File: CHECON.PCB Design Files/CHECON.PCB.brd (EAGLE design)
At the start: 81.7 x 51.6 mm, 71 parts, among them T1 BC849, U2 MAX232SOIC16, U3 RS485SOIC, X1 53047-02

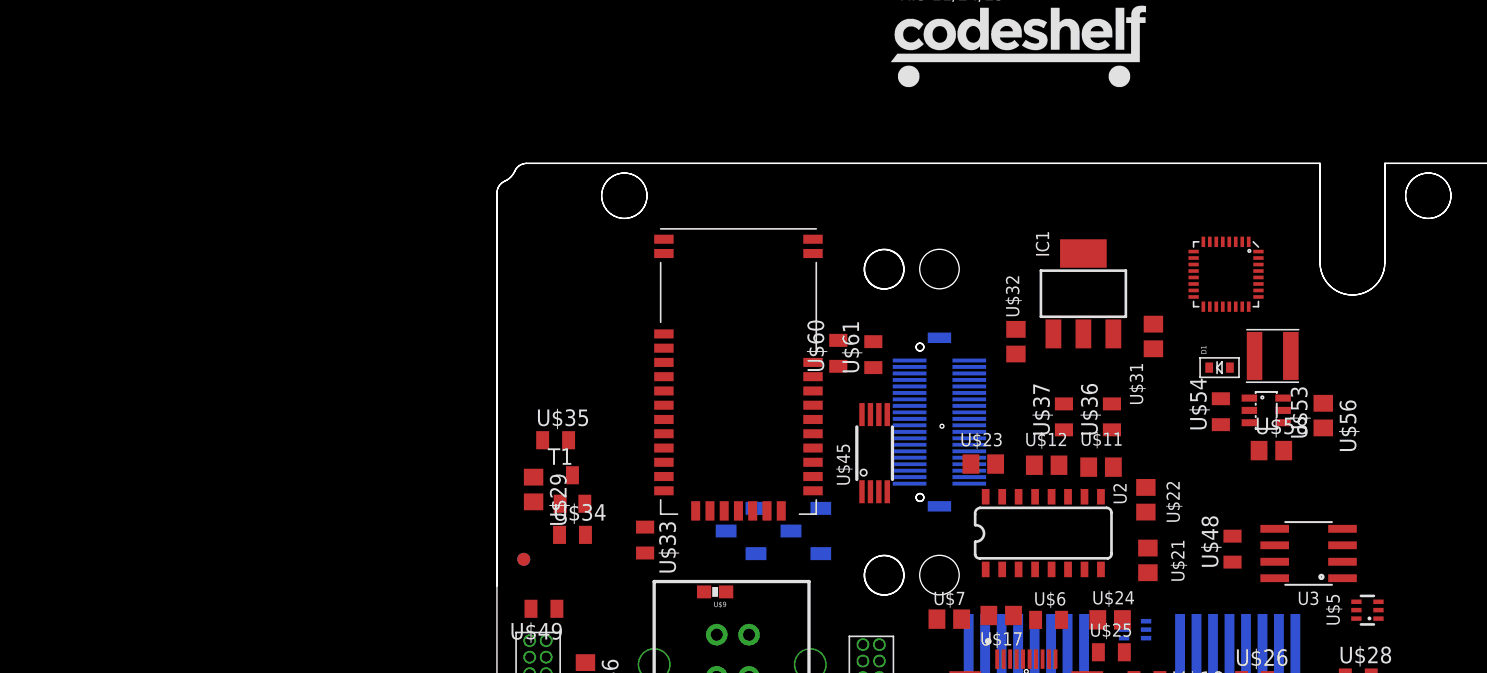
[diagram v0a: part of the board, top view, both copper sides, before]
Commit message: Updated KW2 footprint in design
Swapped footprint for one with 3mm foam outline
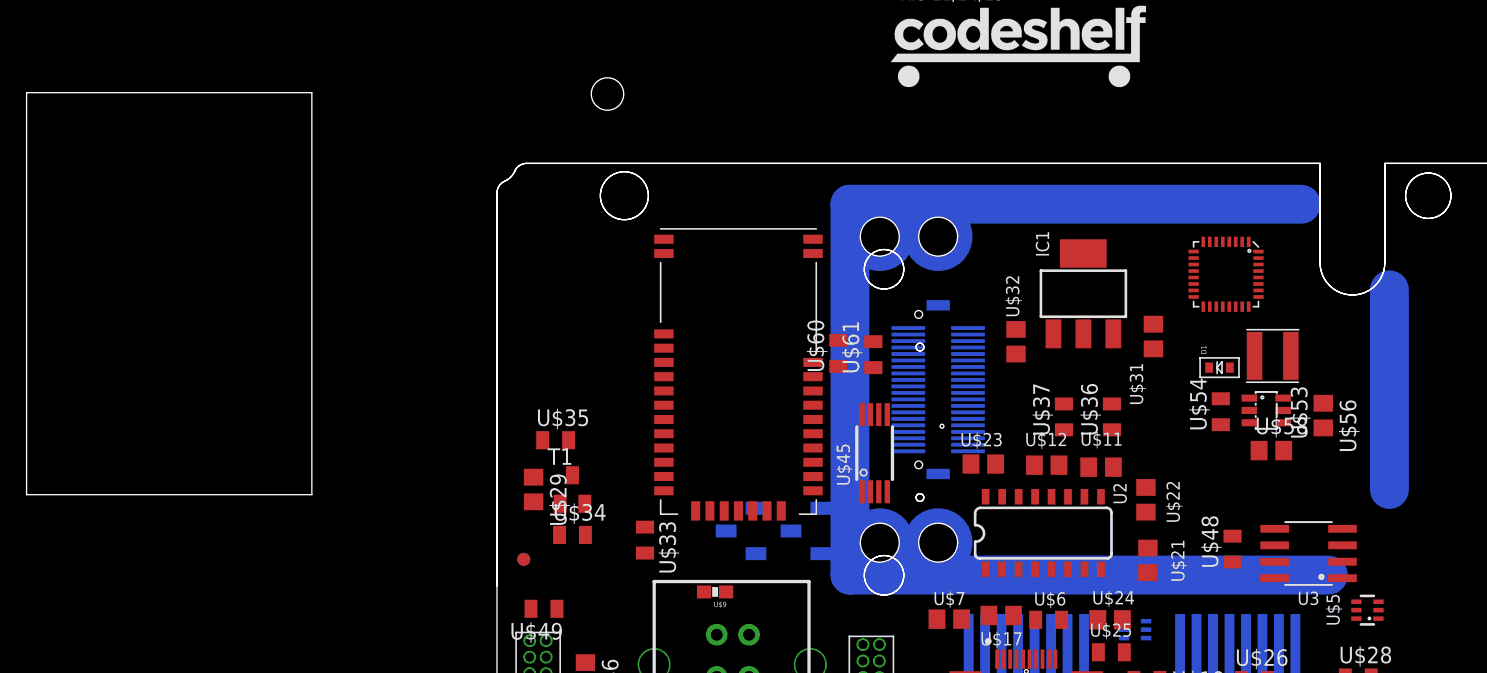
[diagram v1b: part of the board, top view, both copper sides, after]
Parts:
- U$10: value KW2_CPU_COMBO -> KW2_CPU_OFFSET; device KW2:BRAIN_COMBO -> KW2:BRAIN_OFFSET
- moved U$10 2.50 mm to (-6.80, -9.80)
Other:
- board size 81.7 x 51.6 mm -> 117.9 x 57.1 mm

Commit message: sync repo
Sync work while rafael was out
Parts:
- moved U$57 127.9 mm to (-129.6, -88.9)
- moved U$3 68.9 mm to (-46.0, -32.1), turned to 90 degrees
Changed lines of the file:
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@@
 <attribute name="MFGP" value="XD2B-0406-26A" x="-22.8" y="-40.9" size="1.778" layer="27" display="off"/>
 </element>
-<element name="U$3" library="KW2" package="QFN-32" value="KL20" x="15.4" y="-0.9" rot="R270">
-<attribute name="MFGN" value="Freescale" x="15.4" y="-0.9" size="1.778" layer="27" rot="R270" display="off"/>
-<attribute name="MFGP" value="MK20DX128VFM5" x="15.4" y="-0.9" size="1.778" layer="27" rot="R270" display="off"/>
+<element name="U$3" library="KW2" package="QFN-32" value="KL20" x="-46" y="-32.1" rot="R90">
+<attribute name="MFGN" value="Freescale" x="-46" y="-32.1" size="1.778" layer="27" rot="R90" display="off"/>
+<attribute name="MFGP" value="MK20DX128VFM5" x="-46" y="-32.1" size="1.778" layer="27" rot="R90" display="off"/>
 </element>
 <element name="U$9" library="SparkFun" package="0603-RES" value="TVS0603" x="-24" y="-25.4" rot="R180">
@@
 <attribute name="MFGP" value="RC0805FR-0715RL" x="9.3" y="-32.2" size="1.778" layer="27" rot="R180" display="off"/>
 </element>
-<element name="U$57" library="KW2" package="BM78" value="BM78" x="-22.2" y="-19.4"/>
+<element name="U$57" library="KW2" package="BM78" value="BM78" x="-129.6" y="-88.9"/>
 </elements>
 <signals>
@@
 <contactref element="JP1" pad="P$10"/>
 <contactref element="U$3" pad="21"/>
+<wire x1="-12.6" y1="-29.46" x2="-46.25" y2="-29.6" width="0" layer="19" extent="1-1"/>
 <wire x1="-4.5" y1="-6.05" x2="-12.6" y2="-29.46" width="0" layer="19" extent="16-16"/>
-<wire x1="15.65" y1="-3.4" x2="-4.5" y2="-6.05" width="0" layer="19" extent="1-16"/>
-<wire x1="36.9" y1="-36.4" x2="15.65" y2="-3.4" width="0" layer="19" extent="1-1"/>
-<wire x1="30.05" y1="-42.2" x2="36.9" y2="-36.4" width="0" layer="19" extent="1-1"/>
+<wire x1="30.05" y1="-42.2" x2="-12.6" y2="-29.46" width="0" layer="19" extent="1-1"/>
+<wire x1="36.9" y1="-36.4" x2="30.05" y2="-42.2" width="0" layer="19" extent="1-1"/>
 </signal>
 <signal name="GND" class="2">
@@
 <contactref element="U$57" pad="P$2"/>
 <contactref element="U$57" pad="P$3"/>
+<wire x1="-135.35" y1="-68.8" x2="-135.35" y2="-75" width="0" layer="19" extent="1-1"/>
+<wire x1="-135.35" y1="-67.7" x2="-135.35" y2="-68.8" width="0" layer="19" extent="1-1"/>
+<wire x1="-123.85" y1="-68.8" x2="-135.35" y2="-68.8" width="0" layer="19" extent="1-1"/>
+<wire x1="-123.85" y1="-67.7" x2="-123.85" y2="-68.8" width="0" layer="19" extent="1-1"/>
+<wire x1="-123.85" y1="-77.2" x2="-123.85" y2="-68.8" width="0" layer="19" extent="1-1"/>
+<wire x1="-36.3" y1="-39.765" x2="-123.85" y2="-67.7" width="0" layer="19" extent="1-1"/>
 <wire x1="-37.03" y1="-32.97" x2="-36.3" y2="-39.765" width="0" layer="19" extent="1-1"/>
 <wire x1="-37.03" y1="-31.7" x2="-37.03" y2="-32.97" width="0" layer="19" extent="1-1"/>
@@
 <wire x1="2.0886" y1="-5.4988" x2="9.8" y2="-4.75" width="0" layer="19" extent="1-1"/>
 <wire x1="-0.8" y1="-7.05" x2="2.0886" y2="-5.4988" width="0" layer="19" extent="1-1"/>
-<wire x1="-4.5" y1="-5.05" x2="-0.8" y2="-7.05" width="0" layer="19" extent="1-16"/>
-<wire x1="-4.5" y1="-5.55" x2="-4.5" y2="-5.05" width="0" layer="19" extent="16-16"/>
+<wire x1="-4.5" y1="-5.55" x2="-0.8" y2="-7.05" width="0" layer="19" extent="1-16"/>
+<wire x1="-4.5" y1="-5.05" x2="-4.5" y2="-5.55" width="0" layer="19" extent="16-16"/>
 <wire x1="-9.1" y1="-5.55" x2="-4.5" y2="-5.55" width="0" layer="19" extent="16-16"/>
 <wire x1="-9.1" y1="-5.05" x2="-9.1" y2="-5.55" width="0" layer="19" extent="16-16"/>
 <wire x1="-10.7232" y1="-11.7236" x2="-9.1" y2="-5.55" width="0" layer="19" extent="1-16"/>
-<wire x1="-16.45" y1="-7.7" x2="-10.7232" y2="-11.7236" width="0" layer="19" extent="1-1"/>
-<wire x1="-4.27" y1="-15.5364" x2="-4.5" y2="-5.55" width="0" layer="19" extent="1-16"/>
+<wire x1="-4.27" y1="-15.5364" x2="-10.7232" y2="-11.7236" width="0" layer="19" extent="1-1"/>
 <wire x1="-1.865" y1="-18.0624" x2="-4.27" y2="-15.5364" width="0" layer="19" extent="1-1"/>
-<wire x1="-16.45" y1="0.7" x2="-16.45" y2="-7.7" width="0" layer="19" extent="1-1"/>
-<wire x1="-16.45" y1="1.8" x2="-16.45" y2="0.7" width="0" layer="19" extent="1-1"/>
 <wire x1="34.55" y1="-42.2" x2="25.25" y2="-36.3" width="0" layer="19" extent="1-1"/>
-<wire x1="-27.95" y1="1.8" x2="-16.45" y2="1.8" width="0" layer="19" extent="1-1"/>
-<wire x1="-27.95" y1="0.7" x2="-27.95" y2="1.8" width="0" layer="19" extent="1-1"/>
-<wire x1="-27.95" y1="-5.5" x2="-27.95" y2="0.7" width="0" layer="19" extent="1-1"/>
-<wire x1="-37.3" y1="-13.7" x2="-27.95" y2="-5.5" width="0" layer="19" extent="1-1"/>
-<wire x1="-38" y1="-16.55" x2="-37.3" y2="-13.7" width="0" layer="19" extent="1-1"/>
+<wire x1="-38" y1="-16.55" x2="-34" y2="-30.85" width="0" layer="19" extent="1-1"/>
+<wire x1="-37.3" y1="-13.7" x2="-38" y2="-16.55" width="0" layer="19" extent="1-1"/>
 </signal>
 <signal name="+3V3">
@@
 <contactref element="U2" pad="11"/>
 <contactref element="U$10" pad="P$19"/>
-<wire x1="3.215" y1="-18.0624" x2="-9.1" y2="-9.55" width="0" layer="19" extent="1-16"/>
+<wire x1="-9.1" y1="-9.55" x2="3.215" y2="-18.0624" width="0" layer="19" extent="1-16"/>
 </signal>
 <signal name="N$11">
@@
 <contactref element="U$45" pad="7"/>
 <contactref element="U$61" pad="2"/>
-<wire x1="-9.1" y1="-6.55" x2="-12.0232" y2="-11.7236" width="0" layer="19" extent="1-16"/>
-<wire x1="-11.8" y1="-6.1" x2="-9.1" y2="-6.55" width="0" layer="19" extent="1-16"/>
+<wire x1="-11.8" y1="-6.1" x2="-12.0232" y2="-11.7236" width="0" layer="19" extent="1-1"/>
+<wire x1="-9.1" y1="-6.55" x2="-11.8" y2="-6.1" width="0" layer="19" extent="1-16"/>
 </signal>
 <signal name="N$47">
@@
 <contactref element="U$60" pad="2"/>
 <wire x1="-9.1" y1="-7.05" x2="-11.3732" y2="-11.7236" width="0" layer="19" extent="1-16"/>
-<wire x1="-14.5" y1="-6" x2="-11.3732" y2="-11.7236" width="0" layer="19" extent="1-1"/>
+<wire x1="-14.5" y1="-6" x2="-9.1" y2="-7.05" width="0" layer="19" extent="1-16"/>
 </signal>
 <signal name="N$19">
@@
 <contactref element="U$9" pad="2"/>
 <contactref element="U$14" pad="D-"/>
+<wire x1="-23.874" y1="-28.7" x2="-46.25" y2="-34.6" width="0" layer="19" extent="1-1"/>
 <wire x1="-24.85" y1="-25.4" x2="-23.874" y2="-28.7" width="0" layer="19" extent="1-1"/>
-<wire x1="15.65" y1="1.6" x2="-24.85" y2="-25.4" width="0" layer="19" extent="1-1"/>
 </signal>
 <signal name="N$36">
@@
 <contactref element="U$13" pad="2"/>
 <contactref element="U$14" pad="D+"/>
+<wire x1="-25.25" y1="-34" x2="-46.75" y2="-34.6" width="0" layer="19" extent="1-1"/>
 <wire x1="-23.874" y1="-31.95" x2="-25.25" y2="-34" width="0" layer="19" extent="1-1"/>
-<wire x1="16.15" y1="1.6" x2="-23.874" y2="-31.95" width="0" layer="19" extent="1-1"/>
 </signal>
 <signal name="N$5">
@@
 <contactref element="U$47" pad="2"/>
 <contactref element="U$3" pad="15"/>
+<wire x1="-38.3" y1="-34.24" x2="-43.5" y2="-30.85" width="0" layer="19" extent="1-1"/>
 <wire x1="-38" y1="-36.5" x2="-38.3" y2="-34.24" width="0" layer="19" extent="1-1"/>
-<wire x1="12.9" y1="-2.15" x2="-38.3" y2="-34.24" width="0" layer="19" extent="1-1"/>
 </signal>
 <signal name="N$55">
 <contactref element="JP2" pad="P$4"/>
 <contactref element="U$3" pad="12"/>
-<wire x1="12.9" y1="-0.65" x2="-38.3" y2="-32.97" width="0" layer="19" extent="1-1"/>
+<wire x1="-38.3" y1="-32.97" x2="-43.5" y2="-32.35" width="0" layer="19" extent="1-1"/>
 </signal>
 <signal name="N$56">
 <contactref element="JP2" pad="P$6"/>
 <contactref element="U$3" pad="14"/>
-<wire x1="12.9" y1="-1.65" x2="-38.3" y2="-31.7" width="0" layer="19" extent="1-1"/>
+<wire x1="-38.3" y1="-31.7" x2="-43.5" y2="-31.35" width="0" layer="19" extent="1-1"/>
 </signal>
 <signal name="N$57">
 <contactref element="U$3" pad="13"/>
 <contactref element="JP2" pad="P$8"/>
-<wire x1="12.9" y1="-1.15" x2="-38.3" y2="-30.43" width="0" layer="19" extent="1-1"/>
+<wire x1="-38.3" y1="-30.43" x2="-43.5" y2="-31.85" width="0" layer="19" extent="1-1"/>
 </signal>
 <signal name="N$58">
@@
 <contactref element="U$49" pad="2"/>
 <contactref element="JP2" pad="P$10"/>
+<wire x1="-38.3" y1="-29.16" x2="-45.25" y2="-29.6" width="0" layer="19" extent="1-1"/>
 <wire x1="-38.2" y1="-26.7" x2="-38.3" y2="-29.16" width="0" layer="19" extent="1-1"/>
-<wire x1="14.65" y1="-3.4" x2="-38.2" y2="-26.7" width="0" layer="19" extent="1-1"/>
 </signal>
 <signal name="N$1">

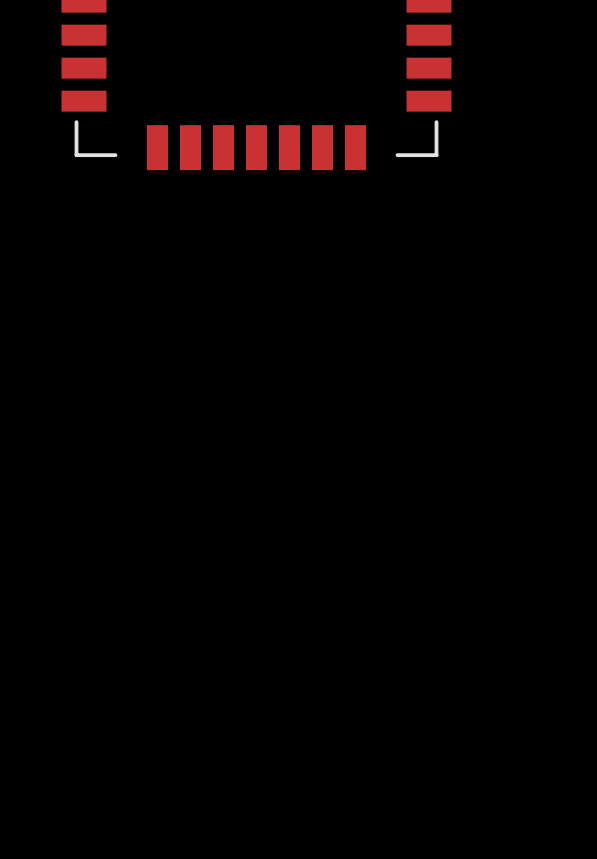
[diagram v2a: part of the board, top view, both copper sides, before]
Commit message: Minor changes
Renamed some nets and worked on SWD section
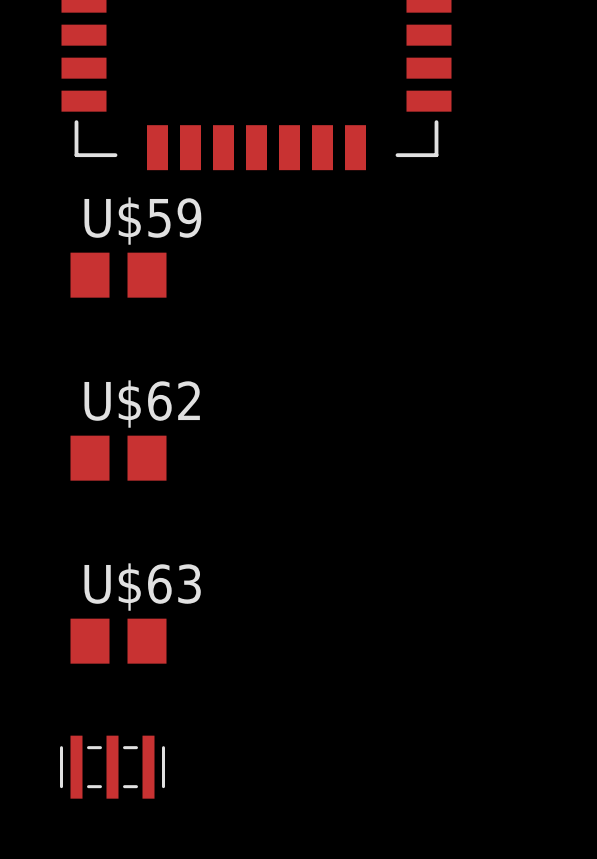
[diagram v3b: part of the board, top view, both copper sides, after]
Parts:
- added U$59: 0.1uF, GW-devices:C0805
- added U$62: 1uF, GW-devices:C0805
- added U$63: 10uF, GW-devices:C0805
- added U$64: CSTCE8M00G55-R0, KW2:CSTCE_G_A
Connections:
- net N$1 renamed SWD_DIO
- net N$4 renamed SWD_CLK
- net N$6 renamed RST
- new net N$1: U$3.27, U$3.28, U$50.P$3
- new net N$4: U$3.17, U$64.P$1
- new net N$6: U$3.18, U$64.P$3
- new net SWD_TGT_CLK: U$3.26, U$51.P$3
- net +3V3: now also U$3.1, U$3.7, U$59.2, U$62.2, U$63.2
- net GND: now also U$3.2, U$3.8, U$59.1, U$62.1, U$63.1, U$64.P$2
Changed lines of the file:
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@@
 <?xml version="1.0" encoding="utf-8"?>
 <!DOCTYPE eagle SYSTEM "eagle.dtd">
-<eagle version="6.6.0">
+<eagle version="7.5.0">
 <drawing>
 <settings>
@@
 <pass name="Default">
 <param name="RoutingGrid" value="50mil"/>
+<param name="AutoGrid" value="1"/>
+<param name="Efforts" value="0"/>
+<param name="TopRouterVariant" value="1"/>
 <param name="tpViaShape" value="round"/>
 <param name="PrefDir.1" value="|"/>
@@
 </element>
 <element name="U$57" library="KW2" package="BM78" value="BM78" x="-129.6" y="-88.9"/>
+<element name="U$59" library="GW-devices" package="C0805" value="0.1uF" x="-134.2" y="-92.9">
+<attribute name="MFGN" value="TDK" x="-134.2" y="-92.9" size="1.778" layer="27" display="off"/>
+<attribute name="MFGP" value="C2012X5R1H104K085AA" x="-134.2" y="-92.9" size="1.778" layer="27" display="off"/>
+</element>
+<element name="U$62" library="GW-devices" package="C0805" value="1uF" x="-134.2" y="-99">
+<attribute name="MFGN" value="TDK" x="-134.2" y="-99" size="1.778" layer="27" display="off"/>
+<attribute name="MFGP" value="C2012X5R1E105K125AA" x="-134.2" y="-99" size="1.778" layer="27" display="off"/>
+</element>
+<element name="U$63" library="GW-devices" package="C0805" value="10uF" x="-134.2" y="-105.1">
+<attribute name="MFGN" value="Murata" x="-134.2" y="-105.1" size="1.778" layer="27" display="off"/>
+<attribute name="MFGP" value="GRM219R61E106KA12D" x="-134.2" y="-105.1" size="1.778" layer="27" display="off"/>
+</element>
+<element name="U$64" library="KW2" package="CSTCE_G_A" value="CSTCE8M00G55-R0" x="-134.4" y="-109.3"/>
 </elements>
 <signals>
-<signal name="N$4">
+<signal name="SWD_CLK">
 <contactref element="U$10" pad="P$8"/>
 <contactref element="JP1" pad="P$4"/>
@@
 <wire x1="-4.5" y1="-6.55" x2="-23.15" y2="-20.7" width="0" layer="19" extent="16-16"/>
 </signal>
-<signal name="N$6">
+<signal name="RST">
 <contactref element="U$10" pad="P$6"/>
 <contactref element="U$30" pad="P$2"/>
@@
 <contactref element="U$57" pad="P$2"/>
 <contactref element="U$57" pad="P$3"/>
+<contactref element="U$3" pad="8"/>
+<contactref element="U$3" pad="2"/>
+<contactref element="U$63" pad="1"/>
+<contactref element="U$62" pad="1"/>
+<contactref element="U$59" pad="1"/>
+<contactref element="U$64" pad="P$2"/>
+<wire x1="-135.15" y1="-105.1" x2="-134.4" y2="-109.3" width="0" layer="19" extent="1-1"/>
+<wire x1="-135.15" y1="-99" x2="-135.15" y2="-105.1" width="0" layer="19" extent="1-1"/>
+<wire x1="-135.15" y1="-92.9" x2="-135.15" y2="-99" width="0" layer="19" extent="1-1"/>
+<wire x1="-135.35" y1="-75" x2="-135.15" y2="-92.9" width="0" layer="19" extent="1-1"/>
 <wire x1="-135.35" y1="-68.8" x2="-135.35" y2="-75" width="0" layer="19" extent="1-1"/>
 <wire x1="-135.35" y1="-67.7" x2="-135.35" y2="-68.8" width="0" layer="19" extent="1-1"/>
@@
 <wire x1="-123.85" y1="-67.7" x2="-123.85" y2="-68.8" width="0" layer="19" extent="1-1"/>
 <wire x1="-123.85" y1="-77.2" x2="-123.85" y2="-68.8" width="0" layer="19" extent="1-1"/>
-<wire x1="-36.3" y1="-39.765" x2="-123.85" y2="-67.7" width="0" layer="19" extent="1-1"/>
-<wire x1="-37.03" y1="-32.97" x2="-36.3" y2="-39.765" width="0" layer="19" extent="1-1"/>
+<wire x1="-47.25" y1="-34.6" x2="-123.85" y2="-67.7" width="0" layer="19" extent="1-1"/>
+<wire x1="-44.25" y1="-34.6" x2="-47.25" y2="-34.6" width="0" layer="19" extent="1-1"/>
+<wire x1="-37.03" y1="-32.97" x2="-44.25" y2="-34.6" width="0" layer="19" extent="1-1"/>
 <wire x1="-37.03" y1="-31.7" x2="-37.03" y2="-32.97" width="0" layer="19" extent="1-1"/>
 <wire x1="-34" y1="-30.85" x2="-37.03" y2="-31.7" width="0" layer="19" extent="1-1"/>
+<wire x1="-36.3" y1="-39.765" x2="-37.03" y2="-32.97" width="0" layer="19" extent="1-1"/>
 <wire x1="-27" y1="-40.9" x2="-36.3" y2="-39.765" width="0" layer="19" extent="1-1"/>
 <wire x1="-23.55" y1="-34" x2="-27" y2="-40.9" width="0" layer="19" extent="1-1"/>
@@
 <contactref element="U$55" pad="P$2"/>
 <contactref element="U$58" pad="2"/>
-<wire x1="-37.03" y1="-34.24" x2="-36" y2="-36.5" width="0" layer="19" extent="1-1"/>
+<contactref element="U$3" pad="1"/>
+<contactref element="U$3" pad="7"/>
+<contactref element="U$59" pad="2"/>
+<contactref element="U$62" pad="2"/>
+<contactref element="U$63" pad="2"/>
+<wire x1="-133.25" y1="-99" x2="-133.25" y2="-105.1" width="0" layer="19" extent="1-1"/>
+<wire x1="-133.25" y1="-92.9" x2="-133.25" y2="-99" width="0" layer="19" extent="1-1"/>
+<wire x1="-47.75" y1="-34.6" x2="-133.25" y2="-92.9" width="0" layer="19" extent="1-1"/>
+<wire x1="-44.75" y1="-34.6" x2="-47.75" y2="-34.6" width="0" layer="19" extent="1-1"/>
+<wire x1="-37.03" y1="-34.24" x2="-44.75" y2="-34.6" width="0" layer="19" extent="1-1"/>
+<wire x1="-36" y1="-36.5" x2="-37.03" y2="-34.24" width="0" layer="19" extent="1-1"/>
 <wire x1="-34" y1="-32.75" x2="-37.03" y2="-34.24" width="0" layer="19" extent="1-1"/>
 <wire x1="-36.2" y1="-26.7" x2="-34" y2="-32.75" width="0" layer="19" extent="1-1"/>
@@
 <wire x1="-38.2" y1="-26.7" x2="-38.3" y2="-29.16" width="0" layer="19" extent="1-1"/>
 </signal>
-<signal name="N$1">
+<signal name="SWD_DIO">
 <contactref element="U$10" pad="P$14"/>
 <contactref element="JP1" pad="P$2"/>
@@
 <wire x1="22.9" y1="-12.75" x2="19.8" y2="-11.4" width="0" layer="19" extent="1-1"/>
 </signal>
+<signal name="SWD_TGT_CLK">
+<contactref element="U$3" pad="26"/>
+<contactref element="U$51" pad="P$3"/>
+<wire x1="-20.85" y1="-22.45" x2="-48.5" y2="-30.85" width="0" layer="19" extent="1-16"/>
+</signal>
+<signal name="N$1">
+<contactref element="U$3" pad="27"/>
+<contactref element="U$50" pad="P$3"/>
+<contactref element="U$3" pad="28"/>
+<wire x1="-48.5" y1="-31.85" x2="-48.5" y2="-31.35" width="0" layer="19" extent="1-1"/>
+<wire x1="-15.85" y1="-22.45" x2="-48.5" y2="-31.35" width="0" layer="19" extent="1-16"/>
+</signal>
+<signal name="N$4">
+<contactref element="U$3" pad="17"/>
+<contactref element="U$64" pad="P$1"/>
+<wire x1="-44.25" y1="-29.6" x2="-135.6" y2="-109.3" width="0" layer="19" extent="1-1"/>
+</signal>
+<signal name="N$6">
+<contactref element="U$3" pad="18"/>
+<contactref element="U$64" pad="P$3"/>
+<wire x1="-44.75" y1="-29.6" x2="-133.2" y2="-109.3" width="0" layer="19" extent="1-1"/>
+</signal>
 </signals>
